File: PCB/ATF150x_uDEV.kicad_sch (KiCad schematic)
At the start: 16 parts, among them J1 Conn_02x05_Odd_Even, J2 VERT, J3 VERT, U1 ATF150xASx-xAx44

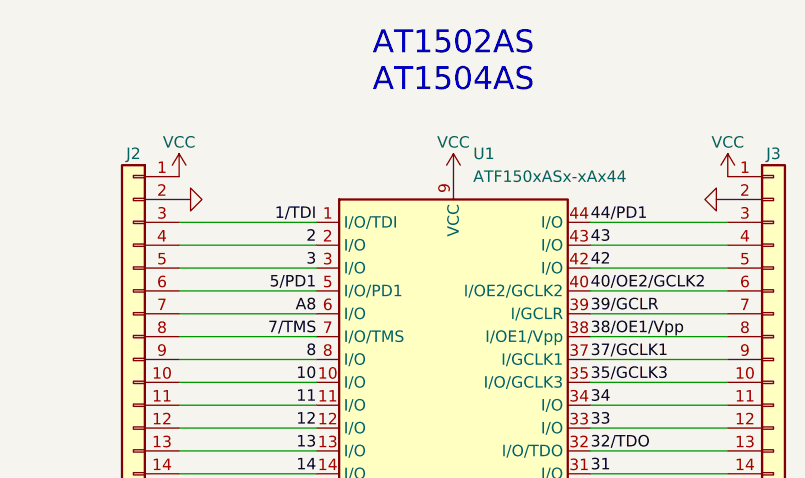
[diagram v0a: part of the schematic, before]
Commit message: fix silkscreen pin 6, remove AS from name & part number
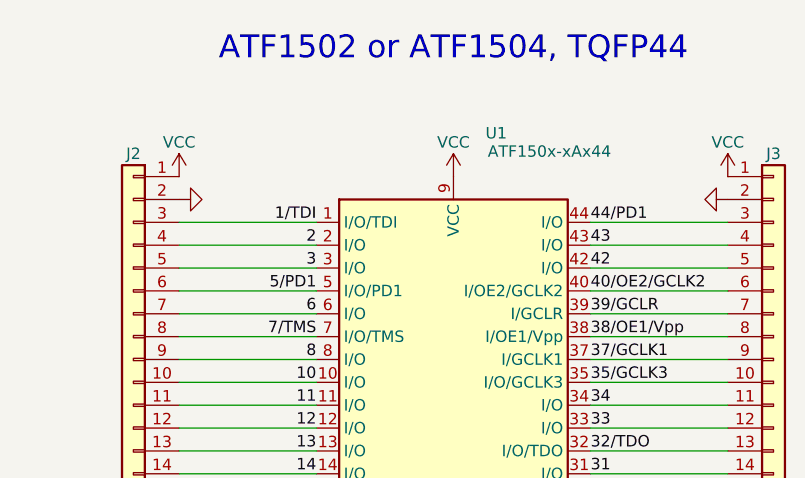
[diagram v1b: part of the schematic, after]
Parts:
- U1: value ATF150xASx-xAx44 -> ATF150x-xAx44; symbol 000_LOCAL:ATF150xASx-xAx44 -> 000_LOCAL:ATF150x-xAx44
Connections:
- net A8 renamed 6
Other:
- note added: "ATF1502 or ATF1504, TQFP44"
- note removed: "AT1502AS AT1504AS"
- title: ATF150xAS_uDEV -> ATF150x_uDEV
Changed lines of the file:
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@@
 	(paper "A4")
 	(title_block
-		(title "ATF150xAS_uDEV")
-		(date "2024-06-14")
-		(rev "003")
+		(title "ATF150x_uDEV")
+		(date "2024-06-23")
+		(rev "004")
 		(company "Brian K. White")
 		(comment 1 "CC-BY-SA")
@@
 		)
 	)
-	(text "AT1502AS\nAT1504AS"
+	(text "ATF1502 or ATF1504, TQFP44\n"
 		(exclude_from_sim no)
 		(at 139.7 50.8 0)
@@
 				(size 2.54 2.54)
 			)
+			(justify bottom)
 		)
 	)
@@
 		)
 	)
-	(label "A8"
+	(label "6"
 		(at 124.46 78.74 180)
 		(fields_autoplaced yes)
@@
 			)
 		)
-		(property "Datasheet" "~"
+		(property "Datasheet" "datasheets/JTAG-A.pdf"
 			(at 62.23 88.9 0)
 			(effects
@@
 	)
 	(symbol
-		(lib_id "000_LOCAL:ATF150xASx-xAx44")
+		(lib_id "000_LOCAL:ATF150x-xAx44")
 		(at 139.7 88.9 0)
 		(unit 1)
@@
 		(on_board yes)
 		(dnp no)
-		(fields_autoplaced yes)
 		(property "Reference" "U1"
-			(at 141.8941 60.96 0)
+			(at 143.256 58.674 0)
 			(effects
 				(font
@@
 			)
 		)
-		(property "Value" "ATF150xASx-xAx44"
-			(at 141.8941 63.5 0)
-			(effects
-				(font
+		(property "Value" "ATF150x-xAx44"
+			(at 143.51 60.706 0)
+			(effects
+				(font

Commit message: jtag symbols
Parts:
- removed J1: Conn_02x05_Odd_Even, 000_LOCAL:IDC-Header_2x05_P2.54mm_Vertical, symbol 000_LOCAL:Conn_02x05_Odd_Even
- added J1: Altera JTAG-A, symbol 000_LOCAL:Altera JTAG-A
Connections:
- net 1/TDI: now also J1.9 (TDI)
- net 26/TCK: now also J1.1 (TCK)
- net 32/TDO: now also J1.3 (TDO)
- net 7/TMS: now also J1.5 (TMS)
- net GND: now also J1.10 (GND), J1.2 (GND)
- net VCC: now also J1.4 (VREF)
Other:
- note removed: "JTAG"
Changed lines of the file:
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@@
 	)
 	(junction
-		(at 71.12 93.98)
+		(at 68.58 93.98)
 		(diameter 0)
 		(color 0 0 0 0)
 	)
 	(no_connect
-		(at 69.85 91.44)
+		(at 67.31 91.44)
 	)
 	(no_connect
-		(at 57.15 91.44)
+		(at 46.99 91.44)
 	)
 	(no_connect
-		(at 69.85 88.9)
+		(at 67.31 88.9)
 	)
 	(wire
@@
 	(wire
 		(pts
-			(xy 71.12 83.82) (xy 71.12 93.98)
+			(xy 68.58 83.82) (xy 68.58 93.98)
 		)
 		(stroke
@@
 	(wire
 		(pts
-			(xy 73.66 86.36) (xy 69.85 86.36)
+			(xy 71.12 86.36) (xy 67.31 86.36)
 		)
 		(stroke
@@
 	(wire
 		(pts
-			(xy 71.12 93.98) (xy 69.85 93.98)
+			(xy 68.58 93.98) (xy 67.31 93.98)
 		)
 		(stroke
@@
 	(wire
 		(pts
-			(xy 69.85 83.82) (xy 71.12 83.82)
+			(xy 67.31 83.82) (xy 68.58 83.82)
 		)
 		(stroke
@@
 		)
 	)
-	(text "JTAG"
-		(exclude_from_sim no)
-		(at 65.532 75.946 0)
-		(effects
-			(font
-				(size 1.27 1.27)
-			)
-			(justify right bottom)
-		)
-	)
 	(label "13"
 		(at 124.46 93.98 180)
@@
 	)
 	(label "32{slash}TDO"
-		(at 57.15 86.36 180)
+		(at 46.99 86.36 180)
 		(fields_autoplaced yes)
 		(effects
@@
 	)
 	(label "26{slash}TCK"
-		(at 57.15 83.82 180)
+		(at 46.99 83.82 180)
 		(fields_autoplaced yes)
 		(effects
@@
 	)
 	(label "1{slash}TDI"
-		(at 57.15 93.98 180)
+		(at 46.99 93.98 180)
 		(fields_autoplaced yes)
 		(effects
@@
 	)
 	(label "7{slash}TMS"
-		(at 57.15 88.9 180)
+		(at 46.99 88.9 180)
 		(fields_autoplaced yes)
 		(effects
@@
 	(symbol
 		(lib_id "power:VCC")
-		(at 73.66 86.36 0)
+		(at 71.12 86.36 0)
 		(unit 1)
 		(exclude_from_sim no)
@@
 		(dnp no)
 		(property "Reference" "#PWR010"
-			(at 73.66 90.17 0)
+			(at 71.12 90.17 0)
 			(effects
 				(font
@@
 		)
 		(property "Value" "VCC"
-			(at 73.66 82.55 0)
+			(at 71.12 82.55 0)
 			(effects
 				(font
@@
 		)
 		(property "Footprint" ""
-			(at 73.66 86.36 0)
+			(at 71.12 86.36 0)
 			(effects
 				(font
@@
 		)
 		(property "Datasheet" ""
-			(at 73.66 86.36 0)
+			(at 71.12 86.36 0)
 			(effects
 				(font
@@
 		)
 		(property "Description" "Power symbol creates a global label with name \"VCC\""
-			(at 73.66 86.36 0)
+			(at 71.12 86.36 0)
 			(effects
 				(font
@@
 				(path "/59fc349f-54da-4a51-bb89-375ab443b404"
 					(reference "#PWR010")
-					(unit 1)
-				)
-			)
-		)
-	)
-	(symbol
-		(lib_id "000_LOCAL:Conn_02x05_Odd_Even")
-		(at 62.23 88.9 0)
-		(unit 1)
-		(exclude_from_sim no)
-		(in_bom yes)
-		(on_board yes)
-		(dnp no)
-		(fields_autoplaced yes)
-		(property "Reference" "J1"
-			(at 63.5 77.47 0)
-			(effects
-				(font
-					(size 1.27 1.27)
-				)
-			)
-		)
-		(property "Value" "Conn_02x05_Odd_Even"
-			(at 63.5 80.01 0)
-			(effects
-				(font
-					(size 1.27 1.27)
-				)
-			)
-		)
-		(property "Footprint" "000_LOCAL:IDC-Header_2x05_P2.54mm_Vertical"
-			(at 62.23 88.9 0)
-			(effects
-				(font
-					(size 1.27 1.27)
-				)
-				(hide yes)
-			)
-		)
-		(property "Datasheet" "datasheets/JTAG-A.pdf"
-			(at 62.23 88.9 0)
-			(effects
-				(font
-					(size 1.27 1.27)
-				)
-				(hide yes)
-			)
-		)
-		(property "Description" "Generic connector, double row, 02x05, odd/even pin numbering scheme (row 1 odd numbers, row 2 even numbers), script generated (kicad-library-utils/schlib/autogen/connector/)"
-			(at 62.23 88.9 0)
-			(effects
-				(font
-					(size 1.27 1.27)
-				)
-				(hide yes)
-			)
-		)
-		(pin "7"
-		)
-		(pin "6"
-		)
-		(pin "5"
-		)
-		(pin "9"
-		)
-		(pin "8"
-		)
-		(pin "1"
-		)
-		(pin "3"
-		)
-		(pin "10"
-		)
-		(pin "2"
-		)
-		(pin "4"
-		)
-		(instances
-			(project "ATF1502AS_uDEV"
-				(path "/59fc349f-54da-4a51-bb89-375ab443b404"
-					(reference "J1")
 					(unit 1)
 				)
@@
 	(symbol
 		(lib_id "power:GND")
-		(at 71.12 93.98 0)
+		(at 68.58 93.98 0)
 		(unit 1)
 		(exclude_from_sim no)
@@
 		(dnp no)
 		(property "Reference" "#PWR01"
-			(at 71.12 100.33 0)
+			(at 68.58 100.33 0)
 			(effects
 				(font
@@
 		)
 		(property "Value" "GND"
-			(at 71.12 98.298 0)
+			(at 68.58 98.298 0)
 			(effects
 				(font
@@
 		)
 		(property "Footprint" ""
-			(at 71.12 93.98 0)
+			(at 68.58 93.98 0)
 			(effects
 				(font
@@
 		)
 		(property "Datasheet" ""
-			(at 71.12 93.98 0)
+			(at 68.58 93.98 0)
 			(effects
 				(font
@@
 		)
 		(property "Description" "Power symbol creates a global label with name \"GND\" , ground"
-			(at 71.12 93.98 0)
+			(at 68.58 93.98 0)
 			(effects
 				(font
@@
 					(unit 1)
 				)
+			)
+		)
+	)
+	(symbol
+		(lib_id "000_LOCAL:Altera JTAG-A")
+		(at 57.15 88.9 0)
+		(unit 1)
+		(exclude_from_sim no)
+		(in_bom yes)
+		(on_board yes)
+		(dnp no)
+		(fields_autoplaced yes)
+		(property "Reference" "J1"
+			(at 57.15 77.47 0)
+			(effects
+				(font
+					(size 1.27 1.27)
+				)
+			)
+		)
+		(property "Value" "Altera JTAG-A"
+			(at 57.15 80.01 0)
+			(effects
+				(font
+					(size 1.27 1.27)
+				)
+			)
+		)
+		(property "Footprint" ""
+			(at 57.15 88.9 0)
+			(effects
+				(font
+					(size 1.27 1.27)
+				)
+				(hide yes)
+			)
+		)
+		(property "Datasheet" "datasheets/JTAG-A.pdf"
+			(at 57.15 88.9 0)
+			(effects
+				(font
+					(size 1.27 1.27)
+				)
+				(hide yes)
+			)
+		)
+		(property "Description" "Generic connector, double row, 02x05, odd/even pin numbering scheme (row 1 odd numbers, row 2 even numbers), script generated (kicad-library-utils/schlib/autogen/connector/)"
+			(at 57.15 88.9 0)
+			(effects
+				(font
+					(size 1.27 1.27)
+				)
+				(hide yes)
+			)
+		)
+		(pin "4"
+		)
+		(pin "7"
+		)
+		(pin "9"
+		)
+		(pin "8"
+		)
+		(pin "2"
+		)
+		(pin "6"
+		)
+		(pin "10"
+		)
+		(pin "1"
+		)
+		(pin "5"
+		)
+		(pin "3"
+		)
+		(instances
+			(project ""
+				(path "/59fc349f-54da-4a51-bb89-375ab443b404"
+					(reference "J1")
+					(unit 1)
+				)

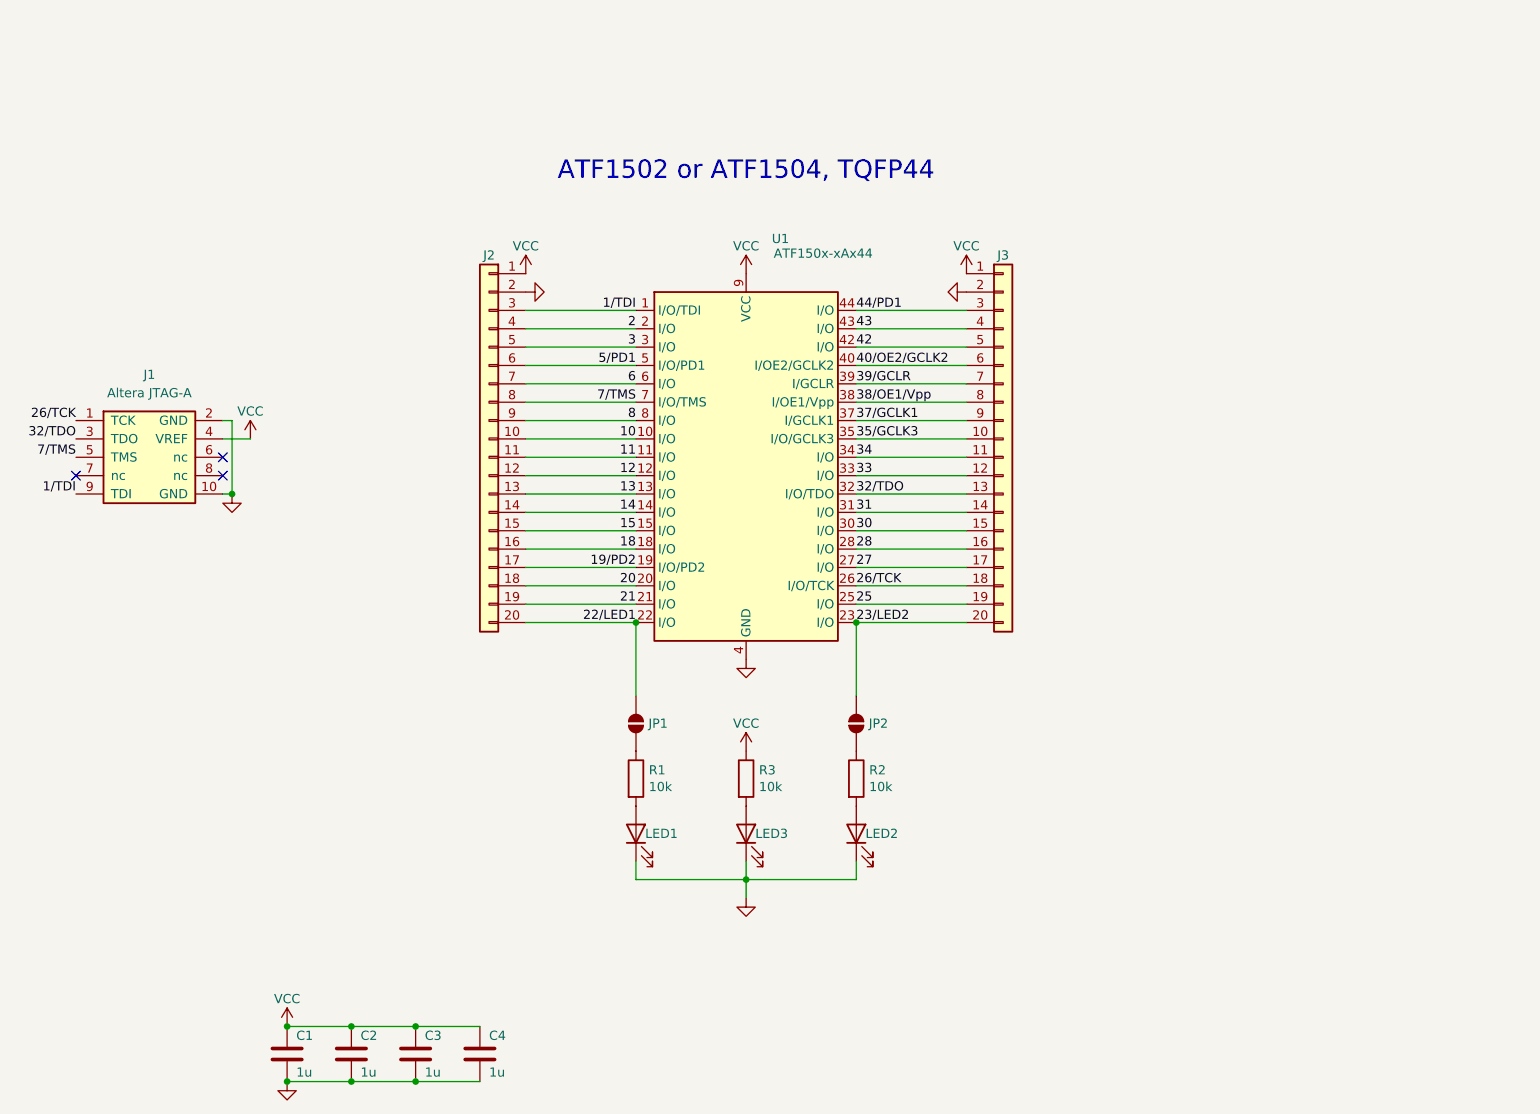
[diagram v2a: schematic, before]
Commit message: add VPP to JTAG
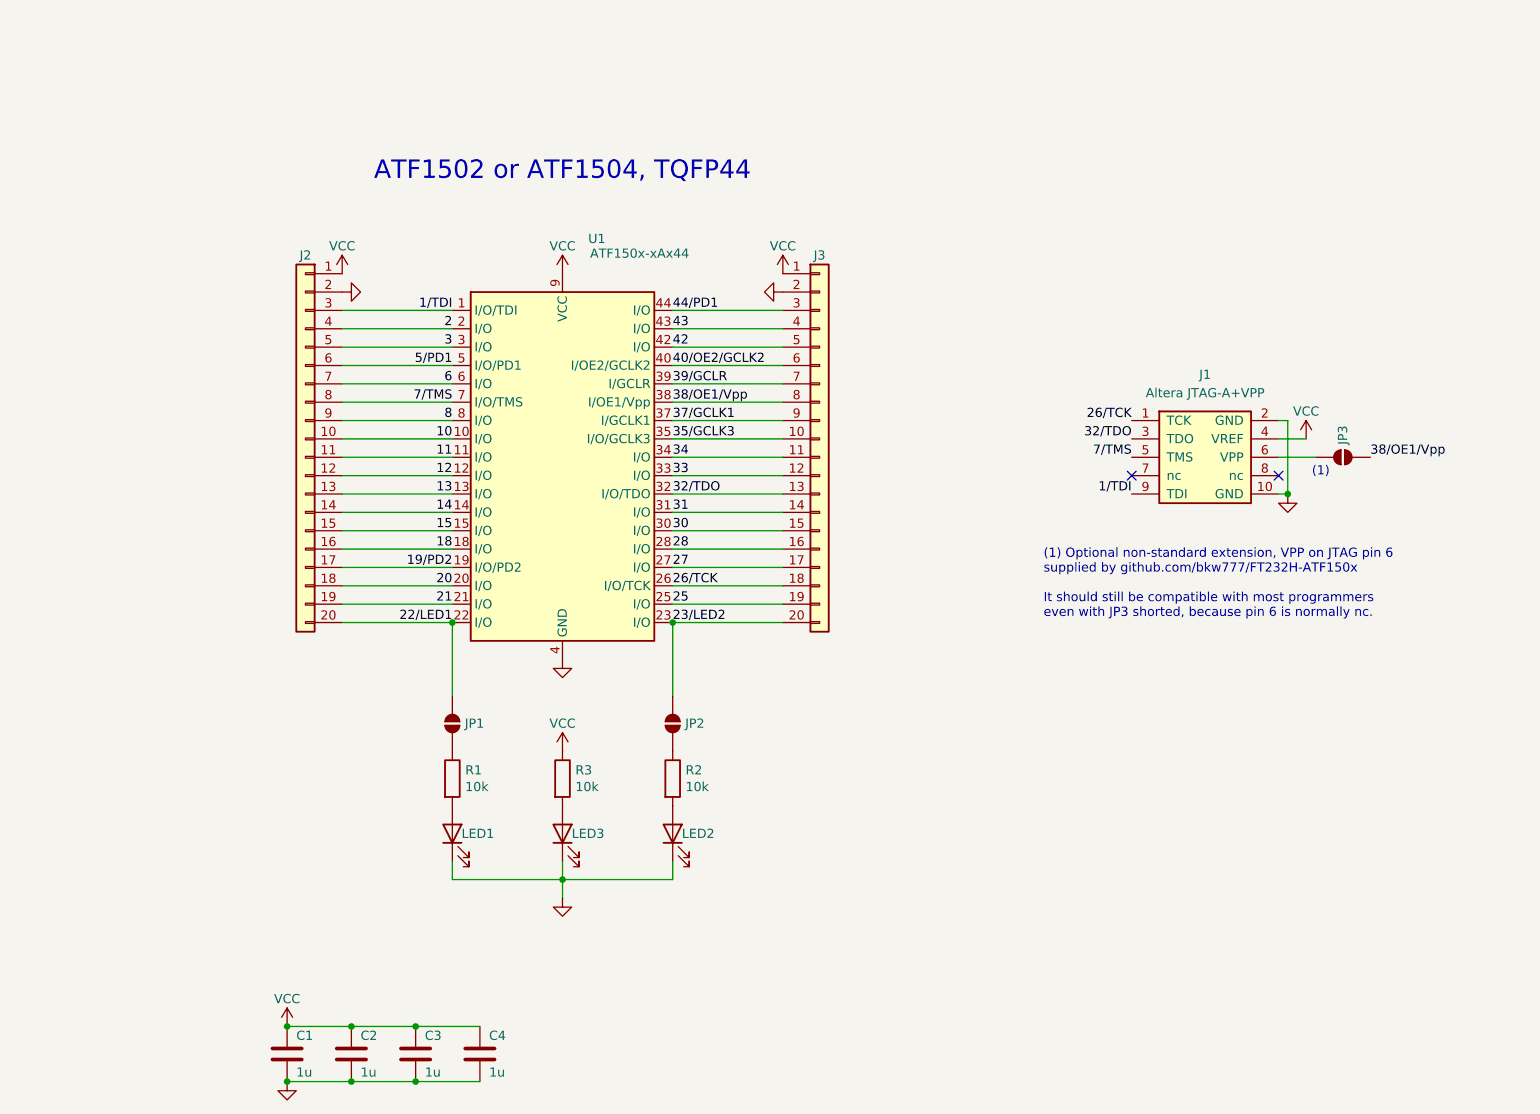
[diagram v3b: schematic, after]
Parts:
- added JP3: DNP, 000_LOCAL:SolderJumper_1mm_2p_open, symbol Jumper:SolderJumper_2_Open
- J1: value Altera JTAG-A -> Altera JTAG-A+VPP; footprint (none) -> 000_LOCAL:IDC-Header_2x05_P2.54mm_Vertical; symbol 000_LOCAL:Altera JTAG-A -> 000_LOCAL:Altera JTAG-A+VPP
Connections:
- net 38/OE1/Vpp: now also JP3.2 (B)
- net at J1.6 (VPP): now also JP3.1 (A)
- no-connect marks 3 -> 2
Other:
- note added: "(1)"
- note added: "(1) Optional non-standard extension, VPP on JTAG pin 6 supplied by github.com/bkw777/FT232H-ATF150x It should still be compatible with most programmers even with JP3 shorted, because pin 6 is normally nc."
- moved on the sheet: J1, J2, J3, JP1, JP2, LED1, LED2, LED3, R1, R2, R3, U1

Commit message: seperate vccio vccint
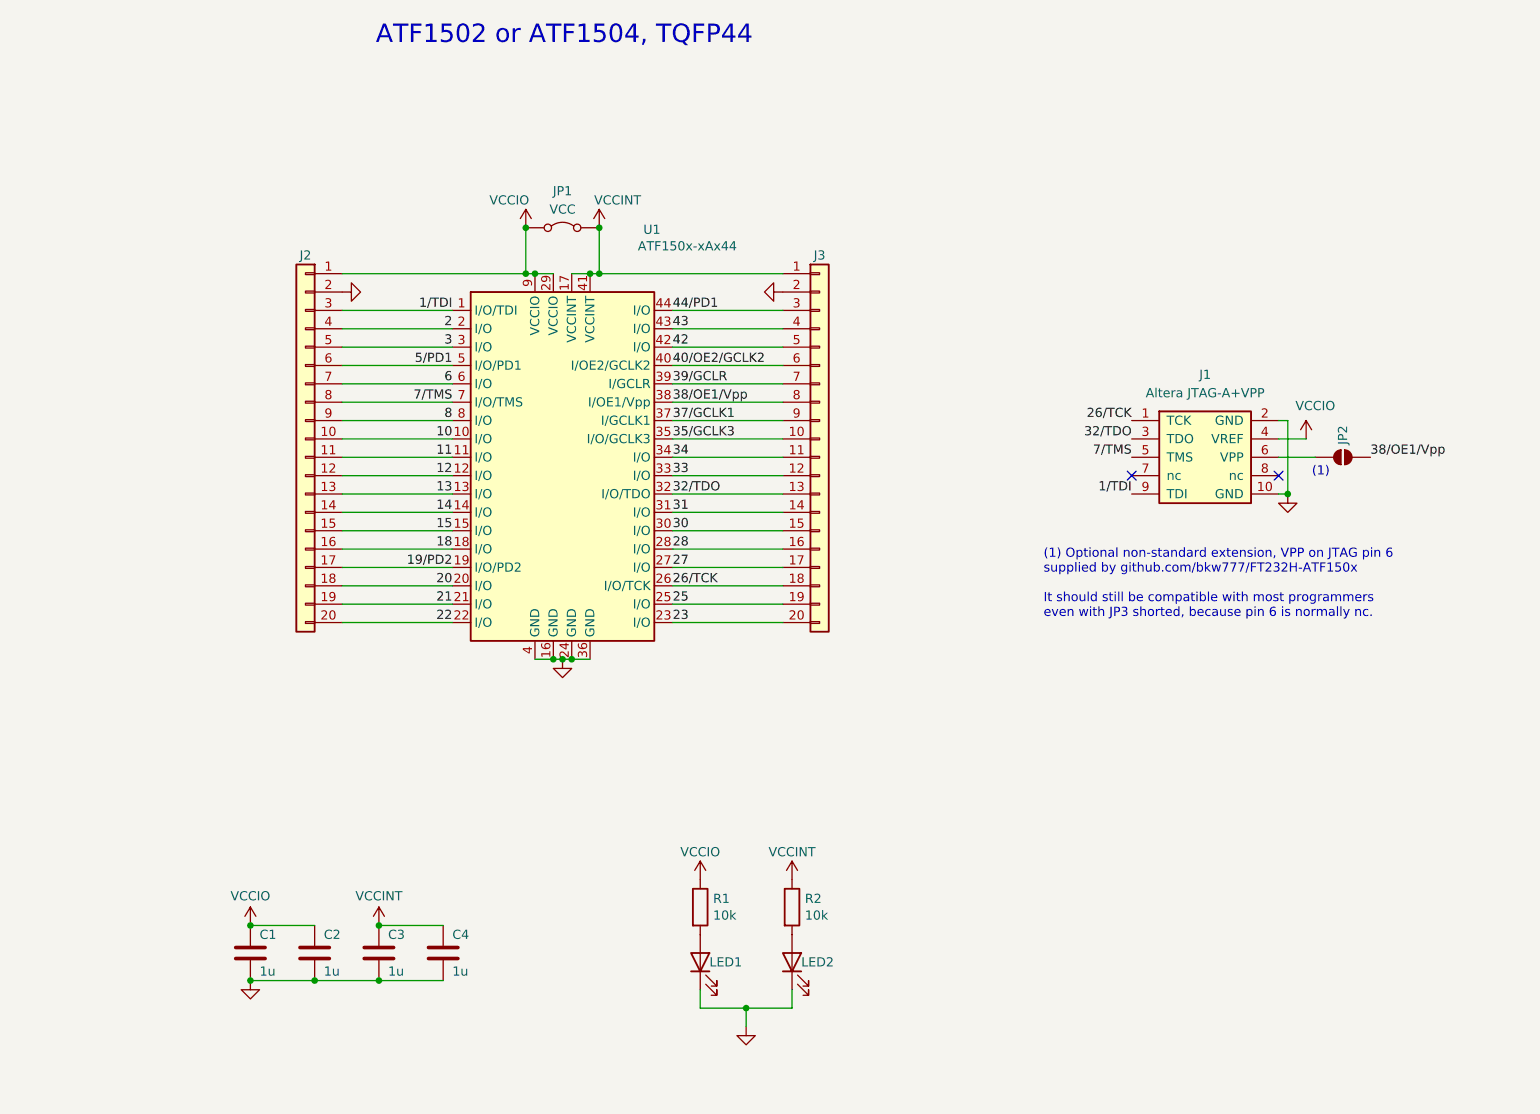
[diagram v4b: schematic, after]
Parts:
- removed JP1, JP2: DNP, 000_LOCAL:SolderJumper_1mm_2p_open, symbol Jumper:SolderJumper_2_Open
- removed LED3: POWER, 000_LOCAL:LED_0805, symbol Device:LED
- removed R3: 10k, 000_LOCAL:R_0805, symbol Device:R
- added JP1: VCC, 000_LOCAL:PinHeader_1x02_P2.54mm_Horizontal, symbol Jumper:Jumper_2_Bridged
- renumbered JP3 to JP2
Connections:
- net VCCIO: now reaches R1.1
- net VCCIO: now also C1.1, C2.1, J1.4 (VREF), J2.1 (Pin_1), U1.29 (VCCIO), U1.9 (VCCIO), JP1.2 (B)
- net VCCINT: now reaches R2.1
- net VCCINT: now also C3.1, C4.1, J3.1 (Pin_1), U1.17 (VCCINT), U1.41 (VCCINT), JP1.1 (A)
- net 22/LED1 renamed 22
- net 23/LED2 renamed 23
- removed net VCC: C1.1, C2.1, C3.1, C4.1, J1.4 (VREF), J2.1 (Pin_1), J3.1 (Pin_1), U1.17 (VCC), U1.29 (VCC), U1.41 (VCC), U1.9 (VCC)
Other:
- moved on the sheet: C1, C2, C3, C4, LED1, LED2, R1, R2

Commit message: move jumper to bottom side
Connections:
- net VCCINT: now also JP1.2 (B); no longer JP1.1 (A)
- net VCCIO: now also JP1.1 (A); no longer JP1.2 (B)
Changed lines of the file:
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@@
 		(lib_id "Jumper:Jumper_2_Bridged")
 		(at 114.3 57.15 0)
-		(mirror y)
 		(unit 1)
 		(exclude_from_sim yes)
